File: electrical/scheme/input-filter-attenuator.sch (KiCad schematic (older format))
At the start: 13 parts, among them U4 AD8672

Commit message: a
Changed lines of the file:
@@
 AR Path="/55AAFE8D/55A8C542" Ref="U6"  Part="1"
 AR Path="/55AAFE9C/55A8C542" Ref="U7"  Part="1"
-F 0 "U5" H 5600 3650 60  0000 C CNN
+F 0 "U6" H 5600 3650 60  0000 C CNN
 F 1 "AD8672" H 5600 4050 60  0000 C CNN
 F 2 "Housings_SOIC:SOIC-8_3.9x4.9mm_Pitch1.27mm" H 5300 3850 60  0001 C CNN
@@
 AR Path="/55AAFE8D/55A8C549" Ref="U6"  Part="2"
 AR Path="/55AAFE9C/55A8C549" Ref="U7"  Part="2"
-F 0 "U5" H 8700 3850 60  0000 C CNN
+F 0 "U6" H 8700 3850 60  0000 C CNN
 F 1 "AD8672" H 8700 4250 60  0000 C CNN
 F 2 "Housings_SOIC:SOIC-8_3.9x4.9mm_Pitch1.27mm" H 8400 4050 60  0001 C CNN
@@
 AR Path="/55AAFE8D/55A8C74B" Ref="R57"  Part="1"
 AR Path="/55AAFE9C/55A8C74B" Ref="R63"  Part="1"
-F 0 "R51" V 5330 2800 50  0000 C CNN
+F 0 "R57" V 5330 2800 50  0000 C CNN
 F 1 "16 5%" V 5250 2800 50  0000 C CNN
 F 2 "Resistors_SMD:R_0805_HandSoldering" V 5180 2800 30  0001 C CNN
@@
 AR Path="/55AAFE8D/55A8C77D" Ref="C54"  Part="1"
 AR Path="/55AAFE9C/55A8C77D" Ref="C60"  Part="1"
-F 0 "C48" H 5025 3150 50  0000 L CNN
+F 0 "C54" H 5025 3150 50  0000 L CNN
 F 1 "100n" H 5025 2950 50  0000 L CNN
 F 2 "Capacitors_SMD:C_0805_HandSoldering" H 5038 2900 30  0001 C CNN
@@
 AR Path="/55AAFE8D/55A8C85F" Ref="#PWR0147"  Part="1"
 AR Path="/55AAFE9C/55A8C85F" Ref="#PWR0153"  Part="1"
-F 0 "#PWR0153" H 4650 2900 50  0001 C CNN
+F 0 "#PWR0147" H 4650 2900 50  0001 C CNN
 F 1 "GNDA" H 4650 3000 50  0000 C CNN
 F 2 "" H 4650 3150 60  0000 C CNN
@@
 AR Path="/55AAFE8D/55A8C8A7" Ref="R58"  Part="1"
 AR Path="/55AAFE9C/55A8C8A7" Ref="R64"  Part="1"
-F 0 "R52" V 5330 4800 50  0000 C CNN
+F 0 "R58" V 5330 4800 50  0000 C CNN
 F 1 "16 5%" V 5250 4800 50  0000 C CNN
 F 2 "Resistors_SMD:R_0805_HandSoldering" V 5180 4800 30  0001 C CNN
@@
 AR Path="/55AAFE8D/55A8CC9D" Ref="C55"  Part="1"
 AR Path="/55AAFE9C/55A8CC9D" Ref="C61"  Part="1"
-F 0 "C49" H 5025 4650 50  0000 L CNN
+F 0 "C55" H 5025 4650 50  0000 L CNN
 F 1 "100n" H 5025 4450 50  0000 L CNN
 F 2 "Capacitors_SMD:C_0805_HandSoldering" H 5038 4400 30  0001 C CNN
@@
 AR Path="/55AAFE8D/55A8CCA5" Ref="#PWR0148"  Part="1"
 AR Path="/55AAFE9C/55A8CCA5" Ref="#PWR0154"  Part="1"
-F 0 "#PWR0154" H 4650 4400 50  0001 C CNN
+F 0 "#PWR0148" H 4650 4400 50  0001 C CNN
 F 1 "GNDA" H 4650 4500 50  0000 C CNN
 F 2 "" H 4650 4650 60  0000 C CNN
@@
 AR Path="/55AAFE8D/55A8D6B2" Ref="R55"  Part="1"
 AR Path="/55AAFE9C/55A8D6B2" Ref="R61"  Part="1"
-F 0 "R49" V 3180 3650 50  0000 C CNN
+F 0 "R55" V 3180 3650 50  0000 C CNN
 F 1 "806 1%" V 3100 3650 50  0000 C CNN
 F 2 "Resistors_SMD:R_0805_HandSoldering" V 3030 3650 30  0001 C CNN
@@
 AR Path="/55AAFE8D/55A8D707" Ref="R56"  Part="1"
 AR Path="/55AAFE9C/55A8D707" Ref="R62"  Part="1"
-F 0 "R50" V 3680 3650 50  0000 C CNN
+F 0 "R56" V 3680 3650 50  0000 C CNN
 F 1 "1k91 1%" V 3600 3650 50  0000 C CNN
 F 2 "Resistors_SMD:R_0805_HandSoldering" V 3530 3650 30  0001 C CNN
@@
 AR Path="/55AAFE8D/55A8D733" Ref="C53"  Part="1"
 AR Path="/55AAFE9C/55A8D733" Ref="C59"  Part="1"
-F 0 "C47" H 3875 4000 50  0000 L CNN
+F 0 "C53" H 3875 4000 50  0000 L CNN
 F 1 "22n" H 3875 3800 50  0000 L CNN
 F 2 "Capacitors_SMD:C_0805_HandSoldering" H 3888 3750 30  0001 C CNN
@@
 AR Path="/55AAFE8D/55A8D76D" Ref="C52"  Part="1"
 AR Path="/55AAFE9C/55A8D76D" Ref="C58"  Part="1"
-F 0 "C46" H 3375 3450 50  0000 L CNN
+F 0 "C52" H 3375 3450 50  0000 L CNN
 F 1 "3u3" H 3375 3250 50  0000 L CNN
 F 2 "Capacitors_SMD:C_0805_HandSoldering" H 3388 3200 30  0001 C CNN
@@
 AR Path="/55AAFE8D/55A8D8D4" Ref="R59"  Part="1"
 AR Path="/55AAFE9C/55A8D8D4" Ref="R65"  Part="1"
-F 0 "R53" V 6280 3850 50  0000 C CNN
+F 0 "R59" V 6280 3850 50  0000 C CNN
 F 1 "9k31 1%" V 6200 3850 50  0000 C CNN
 F 2 "Resistors_SMD:R_0805_HandSoldering" V 6130 3850 30  0001 C CNN
@@
 AR Path="/55AAFE8D/55A8DA7D" Ref="R60"  Part="1"
 AR Path="/55AAFE9C/55A8DA7D" Ref="R66"  Part="1"
-F 0 "R54" V 6780 3850 50  0000 C CNN
+F 0 "R60" V 6780 3850 50  0000 C CNN
 F 1 "21k 1%" V 6700 3850 50  0000 C CNN
 F 2 "Resistors_SMD:R_0805_HandSoldering" V 6630 3850 30  0001 C CNN
@@
 AR Path="/55AAFE8D/55A8DD2D" Ref="C56"  Part="1"
 AR Path="/55AAFE9C/55A8DD2D" Ref="C62"  Part="1"
-F 0 "C50" H 6475 3700 50  0000 L CNN
+F 0 "C56" H 6475 3700 50  0000 L CNN
 F 1 "120n" H 6475 3500 50  0000 L CNN
 F 2 "Capacitors_SMD:C_0805_HandSoldering" H 6488 3450 30  0001 C CNN
@@
 AR Path="/55AAFE8D/55A8DF47" Ref="C57"  Part="1"
 AR Path="/55AAFE9C/55A8DF47" Ref="C63"  Part="1"
-F 0 "C51" H 7075 4300 50  0000 L CNN
+F 0 "C57" H 7075 4300 50  0000 L CNN
 F 1 "22n" H 7075 4100 50  0000 L CNN
 F 2 "Capacitors_SMD:C_0805_HandSoldering" H 7088 4050 30  0001 C CNN
@@
 AR Path="/55AAFE8D/55A8F5C0" Ref="#PWR0149"  Part="1"
 AR Path="/55AAFE9C/55A8F5C0" Ref="#PWR0155"  Part="1"
-F 0 "#PWR0155" H 7050 4300 50  0001 C CNN
+F 0 "#PWR0149" H 7050 4300 50  0001 C CNN
 F 1 "GNDA" H 7050 4400 50  0000 C CNN
 F 2 "" H 7050 4550 60  0000 C CNN
@@
 AR Path="/55AAFE8D/55A8F5EF" Ref="#PWR0150"  Part="1"
 AR Path="/55AAFE9C/55A8F5EF" Ref="#PWR0156"  Part="1"
-F 0 "#PWR0156" H 3850 4000 50  0001 C CNN
+F 0 "#PWR0150" H 3850 4000 50  0001 C CNN
 F 1 "GNDA" H 3850 4100 50  0000 C CNN
 F 2 "" H 3850 4250 60  0000 C CNN
@@
 AR Path="/55AAFE8D/55BB3EFD" Ref="#FLG0151"  Part="1"
 AR Path="/55AAFE9C/55BB3EFD" Ref="#FLG0157"  Part="1"
-F 0 "#FLG0157" H 5600 3045 50  0001 C CNN
+F 0 "#FLG0151" H 5600 3045 50  0001 C CNN
 F 1 "PWR_FLAG" H 5600 3130 50  0000 C CNN
 F 2 "" H 5600 2950 60  0000 C CNN
@@
 AR Path="/55A8BFF5/55BB3F68" Ref="#FLG0140"  Part="1"
 AR Path="/55AAFE9C/55BB3F68" Ref="#FLG0158"  Part="1"
-F 0 "#FLG0158" H 5600 4745 50  0001 C CNN
+F 0 "#FLG0152" H 5600 4745 50  0001 C CNN
 F 1 "PWR_FLAG" H 5600 4830 50  0000 C CNN
 F 2 "" H 5600 4650 60  0000 C CNN

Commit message: a
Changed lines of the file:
@@
 AR Path="/55AAFE8D/55A8C542" Ref="U6"  Part="1"
 AR Path="/55AAFE9C/55A8C542" Ref="U7"  Part="1"
-F 0 "U6" H 5600 3650 60  0000 C CNN
+F 0 "U7" H 5600 3650 60  0000 C CNN
 F 1 "AD8672" H 5600 4050 60  0000 C CNN
 F 2 "Housings_SOIC:SOIC-8_3.9x4.9mm_Pitch1.27mm" H 5300 3850 60  0001 C CNN
@@
 AR Path="/55AAFE8D/55A8C549" Ref="U6"  Part="2"
 AR Path="/55AAFE9C/55A8C549" Ref="U7"  Part="2"
-F 0 "U6" H 8700 3850 60  0000 C CNN
+F 0 "U7" H 8700 3850 60  0000 C CNN
 F 1 "AD8672" H 8700 4250 60  0000 C CNN
 F 2 "Housings_SOIC:SOIC-8_3.9x4.9mm_Pitch1.27mm" H 8400 4050 60  0001 C CNN
@@
 AR Path="/55AAFE8D/55A8C74B" Ref="R57"  Part="1"
 AR Path="/55AAFE9C/55A8C74B" Ref="R63"  Part="1"
-F 0 "R57" V 5330 2800 50  0000 C CNN
+F 0 "R63" V 5330 2800 50  0000 C CNN
 F 1 "16 5%" V 5250 2800 50  0000 C CNN
 F 2 "Resistors_SMD:R_0805_HandSoldering" V 5180 2800 30  0001 C CNN
@@
 AR Path="/55AAFE8D/55A8C77D" Ref="C54"  Part="1"
 AR Path="/55AAFE9C/55A8C77D" Ref="C60"  Part="1"
-F 0 "C54" H 5025 3150 50  0000 L CNN
+F 0 "C60" H 5025 3150 50  0000 L CNN
 F 1 "100n" H 5025 2950 50  0000 L CNN
 F 2 "Capacitors_SMD:C_0805_HandSoldering" H 5038 2900 30  0001 C CNN
@@
 AR Path="/55AAFE8D/55A8C85F" Ref="#PWR0147"  Part="1"
 AR Path="/55AAFE9C/55A8C85F" Ref="#PWR0153"  Part="1"
-F 0 "#PWR0147" H 4650 2900 50  0001 C CNN
+F 0 "#PWR0153" H 4650 2900 50  0001 C CNN
 F 1 "GNDA" H 4650 3000 50  0000 C CNN
 F 2 "" H 4650 3150 60  0000 C CNN
@@
 AR Path="/55AAFE8D/55A8C8A7" Ref="R58"  Part="1"
 AR Path="/55AAFE9C/55A8C8A7" Ref="R64"  Part="1"
-F 0 "R58" V 5330 4800 50  0000 C CNN
+F 0 "R64" V 5330 4800 50  0000 C CNN
 F 1 "16 5%" V 5250 4800 50  0000 C CNN
 F 2 "Resistors_SMD:R_0805_HandSoldering" V 5180 4800 30  0001 C CNN
@@
 AR Path="/55AAFE8D/55A8CC9D" Ref="C55"  Part="1"
 AR Path="/55AAFE9C/55A8CC9D" Ref="C61"  Part="1"
-F 0 "C55" H 5025 4650 50  0000 L CNN
+F 0 "C61" H 5025 4650 50  0000 L CNN
 F 1 "100n" H 5025 4450 50  0000 L CNN
 F 2 "Capacitors_SMD:C_0805_HandSoldering" H 5038 4400 30  0001 C CNN
@@
 AR Path="/55AAFE8D/55A8CCA5" Ref="#PWR0148"  Part="1"
 AR Path="/55AAFE9C/55A8CCA5" Ref="#PWR0154"  Part="1"
-F 0 "#PWR0148" H 4650 4400 50  0001 C CNN
+F 0 "#PWR0154" H 4650 4400 50  0001 C CNN
 F 1 "GNDA" H 4650 4500 50  0000 C CNN
 F 2 "" H 4650 4650 60  0000 C CNN
@@
 AR Path="/55AAFE8D/55A8D6B2" Ref="R55"  Part="1"
 AR Path="/55AAFE9C/55A8D6B2" Ref="R61"  Part="1"
-F 0 "R55" V 3180 3650 50  0000 C CNN
+F 0 "R61" V 3180 3650 50  0000 C CNN
 F 1 "806 1%" V 3100 3650 50  0000 C CNN
 F 2 "Resistors_SMD:R_0805_HandSoldering" V 3030 3650 30  0001 C CNN
@@
 AR Path="/55AAFE8D/55A8D707" Ref="R56"  Part="1"
 AR Path="/55AAFE9C/55A8D707" Ref="R62"  Part="1"
-F 0 "R56" V 3680 3650 50  0000 C CNN
+F 0 "R62" V 3680 3650 50  0000 C CNN
 F 1 "1k91 1%" V 3600 3650 50  0000 C CNN
 F 2 "Resistors_SMD:R_0805_HandSoldering" V 3530 3650 30  0001 C CNN
@@
 AR Path="/55AAFE8D/55A8D733" Ref="C53"  Part="1"
 AR Path="/55AAFE9C/55A8D733" Ref="C59"  Part="1"
-F 0 "C53" H 3875 4000 50  0000 L CNN
+F 0 "C59" H 3875 4000 50  0000 L CNN
 F 1 "22n" H 3875 3800 50  0000 L CNN
 F 2 "Capacitors_SMD:C_0805_HandSoldering" H 3888 3750 30  0001 C CNN
@@
 AR Path="/55AAFE8D/55A8D76D" Ref="C52"  Part="1"
 AR Path="/55AAFE9C/55A8D76D" Ref="C58"  Part="1"
-F 0 "C52" H 3375 3450 50  0000 L CNN
+F 0 "C58" H 3375 3450 50  0000 L CNN
 F 1 "3u3" H 3375 3250 50  0000 L CNN
 F 2 "Capacitors_SMD:C_0805_HandSoldering" H 3388 3200 30  0001 C CNN
@@
 AR Path="/55AAFE8D/55A8D8D4" Ref="R59"  Part="1"
 AR Path="/55AAFE9C/55A8D8D4" Ref="R65"  Part="1"
-F 0 "R59" V 6280 3850 50  0000 C CNN
+F 0 "R65" V 6280 3850 50  0000 C CNN
 F 1 "9k31 1%" V 6200 3850 50  0000 C CNN
 F 2 "Resistors_SMD:R_0805_HandSoldering" V 6130 3850 30  0001 C CNN
@@
 AR Path="/55AAFE8D/55A8DA7D" Ref="R60"  Part="1"
 AR Path="/55AAFE9C/55A8DA7D" Ref="R66"  Part="1"
-F 0 "R60" V 6780 3850 50  0000 C CNN
+F 0 "R66" V 6780 3850 50  0000 C CNN
 F 1 "21k 1%" V 6700 3850 50  0000 C CNN
 F 2 "Resistors_SMD:R_0805_HandSoldering" V 6630 3850 30  0001 C CNN
@@
 AR Path="/55AAFE8D/55A8DD2D" Ref="C56"  Part="1"
 AR Path="/55AAFE9C/55A8DD2D" Ref="C62"  Part="1"
-F 0 "C56" H 6475 3700 50  0000 L CNN
+F 0 "C62" H 6475 3700 50  0000 L CNN
 F 1 "120n" H 6475 3500 50  0000 L CNN
 F 2 "Capacitors_SMD:C_0805_HandSoldering" H 6488 3450 30  0001 C CNN
@@
 AR Path="/55AAFE8D/55A8DF47" Ref="C57"  Part="1"
 AR Path="/55AAFE9C/55A8DF47" Ref="C63"  Part="1"
-F 0 "C57" H 7075 4300 50  0000 L CNN
+F 0 "C63" H 7075 4300 50  0000 L CNN
 F 1 "22n" H 7075 4100 50  0000 L CNN
 F 2 "Capacitors_SMD:C_0805_HandSoldering" H 7088 4050 30  0001 C CNN
@@
 AR Path="/55AAFE8D/55A8F5C0" Ref="#PWR0149"  Part="1"
 AR Path="/55AAFE9C/55A8F5C0" Ref="#PWR0155"  Part="1"
-F 0 "#PWR0149" H 7050 4300 50  0001 C CNN
+F 0 "#PWR0155" H 7050 4300 50  0001 C CNN
 F 1 "GNDA" H 7050 4400 50  0000 C CNN
 F 2 "" H 7050 4550 60  0000 C CNN
@@
 AR Path="/55AAFE8D/55A8F5EF" Ref="#PWR0150"  Part="1"
 AR Path="/55AAFE9C/55A8F5EF" Ref="#PWR0156"  Part="1"
-F 0 "#PWR0150" H 3850 4000 50  0001 C CNN
+F 0 "#PWR0156" H 3850 4000 50  0001 C CNN
 F 1 "GNDA" H 3850 4100 50  0000 C CNN
 F 2 "" H 3850 4250 60  0000 C CNN
@@
 AR Path="/55AAFE8D/55BB3EFD" Ref="#FLG0151"  Part="1"
 AR Path="/55AAFE9C/55BB3EFD" Ref="#FLG0157"  Part="1"
-F 0 "#FLG0151" H 5600 3045 50  0001 C CNN
+F 0 "#FLG0157" H 5600 3045 50  0001 C CNN
 F 1 "PWR_FLAG" H 5600 3130 50  0000 C CNN
 F 2 "" H 5600 2950 60  0000 C CNN
@@
 AR Path="/55A8BFF5/55BB3F68" Ref="#FLG0140"  Part="1"
 AR Path="/55AAFE9C/55BB3F68" Ref="#FLG0158"  Part="1"
-F 0 "#FLG0152" H 5600 4745 50  0001 C CNN
+F 0 "#FLG0158" H 5600 4745 50  0001 C CNN
 F 1 "PWR_FLAG" H 5600 4830 50  0000 C CNN
 F 2 "" H 5600 4650 60  0000 C CNN

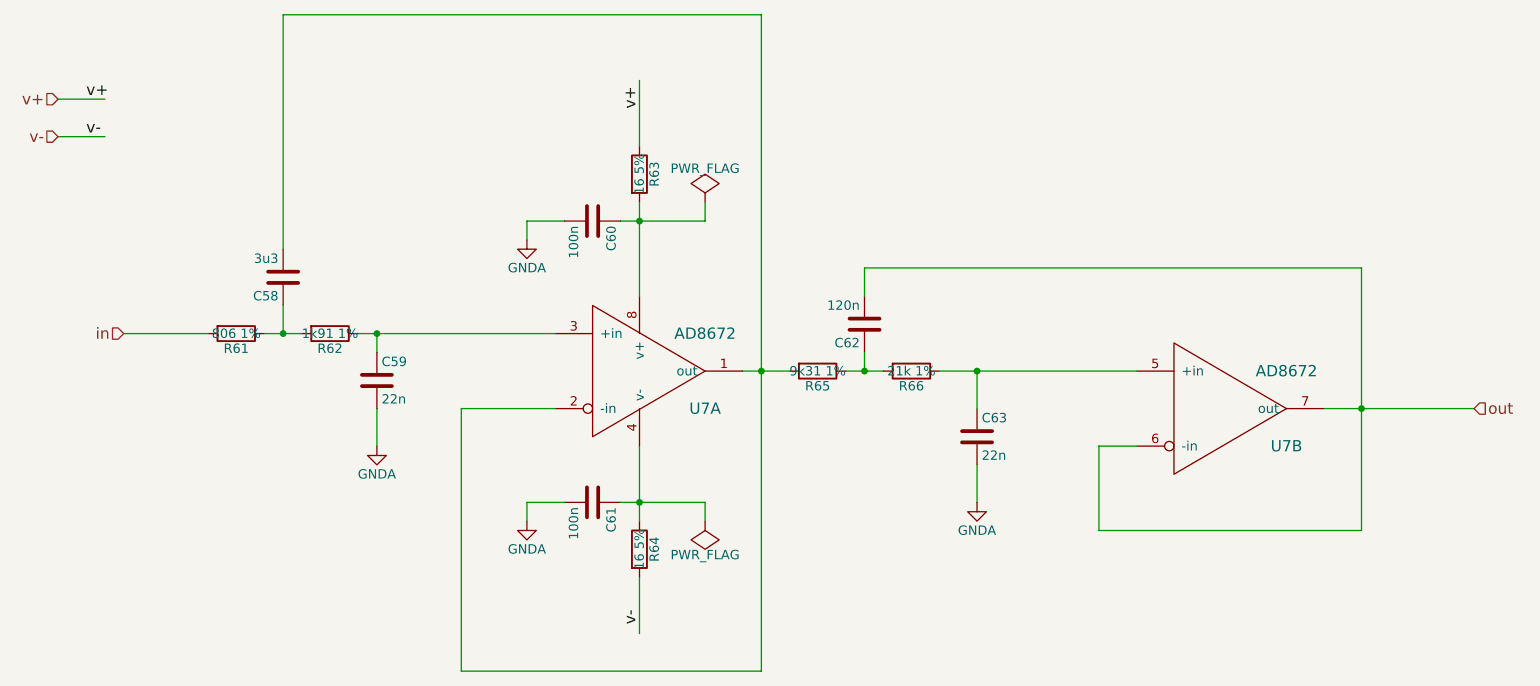
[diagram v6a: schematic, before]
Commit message: Turned out that microcontroller performance is hardly enough to read 20kHz. And changed input filters into 2-d order + buffer to prevent multiplexor switches problem.
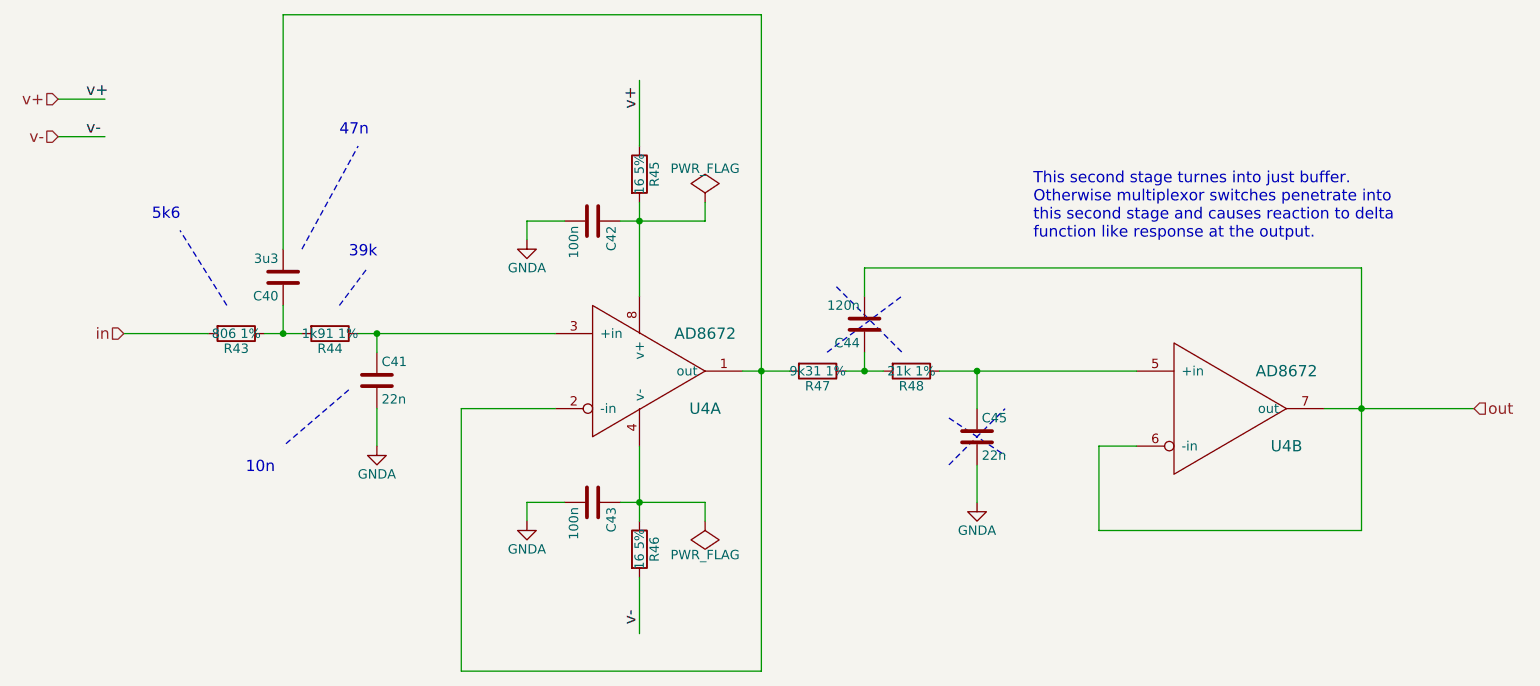
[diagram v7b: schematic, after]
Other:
- note added: "10n"
- note added: "39k"
- note added: "47n"
- note added: "5k6"
- note added: "This second stage turnes into just buffer.\nOtherwise multiplexor switches penetrate into \nthis second stage and causes reaction to delta \nfunction like response at the output."
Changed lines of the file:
@@
 $Descr A4 11693 8268
 encoding utf-8
-Sheet 3 7
+Sheet 2 7
 Title ""
 Date ""
@@
 AR Path="/55AAFE8D/55A8C542" Ref="U6"  Part="1"
 AR Path="/55AAFE9C/55A8C542" Ref="U7"  Part="1"
-F 0 "U7" H 5600 3650 60  0000 C CNN
+F 0 "U4" H 5600 3650 60  0000 C CNN
 F 1 "AD8672" H 5600 4050 60  0000 C CNN
 F 2 "Housings_SOIC:SOIC-8_3.9x4.9mm_Pitch1.27mm" H 5300 3850 60  0001 C CNN
@@
 AR Path="/55AAFE8D/55A8C549" Ref="U6"  Part="2"
 AR Path="/55AAFE9C/55A8C549" Ref="U7"  Part="2"
-F 0 "U7" H 8700 3850 60  0000 C CNN
+F 0 "U4" H 8700 3850 60  0000 C CNN
 F 1 "AD8672" H 8700 4250 60  0000 C CNN
 F 2 "Housings_SOIC:SOIC-8_3.9x4.9mm_Pitch1.27mm" H 8400 4050 60  0001 C CNN
@@
 AR Path="/55AAFE8D/55A8C74B" Ref="R57"  Part="1"
 AR Path="/55AAFE9C/55A8C74B" Ref="R63"  Part="1"
-F 0 "R63" V 5330 2800 50  0000 C CNN
+F 0 "R45" V 5330 2800 50  0000 C CNN
 F 1 "16 5%" V 5250 2800 50  0000 C CNN
 F 2 "Resistors_SMD:R_0805_HandSoldering" V 5180 2800 30  0001 C CNN
@@
 AR Path="/55AAFE8D/55A8C77D" Ref="C54"  Part="1"
 AR Path="/55AAFE9C/55A8C77D" Ref="C60"  Part="1"
-F 0 "C60" H 5025 3150 50  0000 L CNN
+F 0 "C42" H 5025 3150 50  0000 L CNN
 F 1 "100n" H 5025 2950 50  0000 L CNN
 F 2 "Capacitors_SMD:C_0805_HandSoldering" H 5038 2900 30  0001 C CNN
@@
 AR Path="/55AAFE8D/55A8C85F" Ref="#PWR0145"  Part="1"
 AR Path="/55AAFE9C/55A8C85F" Ref="#PWR0151"  Part="1"
-F 0 "#PWR0151" H 4650 2900 50  0001 C CNN
+F 0 "#PWR0133" H 4650 2900 50  0001 C CNN
 F 1 "GNDA" H 4650 3000 50  0000 C CNN
 F 2 "" H 4650 3150 60  0000 C CNN
@@
 AR Path="/55AAFE8D/55A8C8A7" Ref="R58"  Part="1"
 AR Path="/55AAFE9C/55A8C8A7" Ref="R64"  Part="1"
-F 0 "R64" V 5330 4800 50  0000 C CNN
+F 0 "R46" V 5330 4800 50  0000 C CNN
 F 1 "16 5%" V 5250 4800 50  0000 C CNN
 F 2 "Resistors_SMD:R_0805_HandSoldering" V 5180 4800 30  0001 C CNN
@@
 AR Path="/55AAFE8D/55A8CC9D" Ref="C55"  Part="1"
 AR Path="/55AAFE9C/55A8CC9D" Ref="C61"  Part="1"
-F 0 "C61" H 5025 4650 50  0000 L CNN
+F 0 "C43" H 5025 4650 50  0000 L CNN
 F 1 "100n" H 5025 4450 50  0000 L CNN
 F 2 "Capacitors_SMD:C_0805_HandSoldering" H 5038 4400 30  0001 C CNN
@@
 AR Path="/55AAFE8D/55A8CCA5" Ref="#PWR0146"  Part="1"
 AR Path="/55AAFE9C/55A8CCA5" Ref="#PWR0152"  Part="1"
-F 0 "#PWR0152" H 4650 4400 50  0001 C CNN
+F 0 "#PWR0134" H 4650 4400 50  0001 C CNN
 F 1 "GNDA" H 4650 4500 50  0000 C CNN
 F 2 "" H 4650 4650 60  0000 C CNN
@@
 AR Path="/55AAFE8D/55A8D6B2" Ref="R55"  Part="1"
 AR Path="/55AAFE9C/55A8D6B2" Ref="R61"  Part="1"
-F 0 "R61" V 3180 3650 50  0000 C CNN
+F 0 "R43" V 3180 3650 50  0000 C CNN
 F 1 "806 1%" V 3100 3650 50  0000 C CNN
 F 2 "Resistors_SMD:R_0805_HandSoldering" V 3030 3650 30  0001 C CNN
@@
 AR Path="/55AAFE8D/55A8D707" Ref="R56"  Part="1"
 AR Path="/55AAFE9C/55A8D707" Ref="R62"  Part="1"
-F 0 "R62" V 3680 3650 50  0000 C CNN
+F 0 "R44" V 3680 3650 50  0000 C CNN
 F 1 "1k91 1%" V 3600 3650 50  0000 C CNN
 F 2 "Resistors_SMD:R_0805_HandSoldering" V 3530 3650 30  0001 C CNN
@@
 AR Path="/55AAFE8D/55A8D733" Ref="C53"  Part="1"
 AR Path="/55AAFE9C/55A8D733" Ref="C59"  Part="1"
-F 0 "C59" H 3875 4000 50  0000 L CNN
+F 0 "C41" H 3875 4000 50  0000 L CNN
 F 1 "22n" H 3875 3800 50  0000 L CNN
 F 2 "Capacitors_SMD:C_0805_HandSoldering" H 3888 3750 30  0001 C CNN
@@
 AR Path="/55AAFE8D/55A8D76D" Ref="C52"  Part="1"
 AR Path="/55AAFE9C/55A8D76D" Ref="C58"  Part="1"
-F 0 "C58" H 3375 3450 50  0000 L CNN
+F 0 "C40" H 3375 3450 50  0000 L CNN
 F 1 "3u3" H 3375 3250 50  0000 L CNN
 F 2 "Capacitors_SMD:C_0805_HandSoldering" H 3388 3200 30  0001 C CNN
@@
 AR Path="/55AAFE8D/55A8D8D4" Ref="R59"  Part="1"
 AR Path="/55AAFE9C/55A8D8D4" Ref="R65"  Part="1"
-F 0 "R65" V 6280 3850 50  0000 C CNN
+F 0 "R47" V 6280 3850 50  0000 C CNN
 F 1 "9k31 1%" V 6200 3850 50  0000 C CNN
 F 2 "Resistors_SMD:R_0805_HandSoldering" V 6130 3850 30  0001 C CNN
@@
 AR Path="/55AAFE8D/55A8DA7D" Ref="R60"  Part="1"
 AR Path="/55AAFE9C/55A8DA7D" Ref="R66"  Part="1"
-F 0 "R66" V 6780 3850 50  0000 C CNN
+F 0 "R48" V 6780 3850 50  0000 C CNN
 F 1 "21k 1%" V 6700 3850 50  0000 C CNN
 F 2 "Resistors_SMD:R_0805_HandSoldering" V 6630 3850 30  0001 C CNN
@@
 AR Path="/55AAFE8D/55A8DD2D" Ref="C56"  Part="1"
 AR Path="/55AAFE9C/55A8DD2D" Ref="C62"  Part="1"
-F 0 "C62" H 6475 3700 50  0000 L CNN
+F 0 "C44" H 6475 3700 50  0000 L CNN
 F 1 "120n" H 6475 3500 50  0000 L CNN
 F 2 "Capacitors_SMD:C_0805_HandSoldering" H 6488 3450 30  0001 C CNN
@@
 AR Path="/55AAFE8D/55A8DF47" Ref="C57"  Part="1"
 AR Path="/55AAFE9C/55A8DF47" Ref="C63"  Part="1"
-F 0 "C63" H 7075 4300 50  0000 L CNN
+F 0 "C45" H 7075 4300 50  0000 L CNN
 F 1 "22n" H 7075 4100 50  0000 L CNN
 F 2 "Capacitors_SMD:C_0805_HandSoldering" H 7088 4050 30  0001 C CNN
@@
 AR Path="/55AAFE8D/55A8F5C0" Ref="#PWR0147"  Part="1"
 AR Path="/55AAFE9C/55A8F5C0" Ref="#PWR0153"  Part="1"
-F 0 "#PWR0153" H 7050 4300 50  0001 C CNN
+F 0 "#PWR0135" H 7050 4300 50  0001 C CNN
 F 1 "GNDA" H 7050 4400 50  0000 C CNN
 F 2 "" H 7050 4550 60  0000 C CNN
@@
 AR Path="/55AAFE8D/55A8F5EF" Ref="#PWR0148"  Part="1"
 AR Path="/55AAFE9C/55A8F5EF" Ref="#PWR0154"  Part="1"
-F 0 "#PWR0154" H 3850 4000 50  0001 C CNN
+F 0 "#PWR0136" H 3850 4000 50  0001 C CNN
 F 1 "GNDA" H 3850 4100 50  0000 C CNN
 F 2 "" H 3850 4250 60  0000 C CNN
@@
 AR Path="/55AAFE8D/55BB3EFD" Ref="#FLG0149"  Part="1"
 AR Path="/55AAFE9C/55BB3EFD" Ref="#FLG0155"  Part="1"
-F 0 "#FLG0155" H 5600 3045 50  0001 C CNN
+F 0 "#FLG0137" H 5600 3045 50  0001 C CNN
 F 1 "PWR_FLAG" H 5600 3130 50  0000 C CNN
 F 2 "" H 5600 2950 60  0000 C CNN
@@
 AR Path="/55A8BFF5/55BB3F68" Ref="#FLG0138"  Part="1"
 AR Path="/55AAFE9C/55BB3F68" Ref="#FLG0156"  Part="1"
-F 0 "#FLG0156" H 5600 4745 50  0001 C CNN
+F 0 "#FLG0138" H 5600 4745 50  0001 C CNN
 F 1 "PWR_FLAG" H 5600 4830 50  0000 C CNN
 F 2 "" H 5600 4650 60  0000 C CNN
@@
 Wire Wire Line
 	5600 4550 5600 4650
+Wire Notes Line
+	6300 3400 6650 3750
+Wire Notes Line
+	6250 3750 6650 3450
+Wire Notes Line
+	6900 4100 7200 4300
+Wire Notes Line
+	6900 4350 7200 4050
+Wire Notes Line
+	3050 3500 2800 3100
+Text Notes 2650 3050 0    60   ~ 0
+5k6
+Wire Notes Line
+	3650 3500 3800 3300
+Text Notes 3700 3250 0    60   ~ 0
+39k
+Wire Notes Line
+	3700 3950 3350 4250
+Text Notes 3150 4400 0    60   ~ 0
+10n
+Wire Notes Line
+	3450 3200 3750 2650
+Text Notes 3650 2600 0    60   ~ 0
+47n
+Text Notes 7350 3150 0    60   ~ 0
+This second stage turnes into just buffer.\nOtherwise multiplexor switches penetrate into \nthis second stage and causes reaction to delta \nfunction like response at the output.
 $EndSCHEMATC
